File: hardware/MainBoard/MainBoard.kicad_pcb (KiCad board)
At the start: 2 copper layers, 50 x 80 mm, 29 parts, among them J101 Servo, J102 Relay, J103 MotorDriver, J104 MPU9250, J105 PicoBATT+, J106 Tachometer, J201 Micro_SD_Card, SW101 Reset, SW102 SW_Pico, SW103 SW_BATT

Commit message: ちょっと位置修正と，SDの接続ピン変更
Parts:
- moved C201 8.51 mm to (141.8, 97.5), turned to -90 degrees
- moved C202 8.50 mm to (138.7, 97.5), turned to -90 degrees
- moved R201 1.44 mm to (129.2, 106.2)
- moved R202 1.44 mm to (129.2, 103.7)
- moved R203 1.44 mm to (129.2, 101.2)
- moved R204 1.44 mm to (129.2, 98.7)
- moved R102 0.70 mm to (139.0, 111.7)
- moved SW103 0.63 mm to (162.6, 51.7)
- moved SW102 0.60 mm to (162.6, 63.5)
- moved D101 0.50 mm to (120.1, 86.8)
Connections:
- A101 pad 22: /CS -> /CLK
- A101 pad 24: /CLK -> /MOSI
- A101 pad 25: /MOSI -> /CS
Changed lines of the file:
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@@
 	(footprint "Resistor_THT:R_Axial_DIN0204_L3.6mm_D1.6mm_P5.08mm_Horizontal"
 		(layer "F.Cu")
-		(at 130.42 107)
+		(at 129.22 106.2)
 		(descr "Resistor, Axial_DIN0204 series, Axial, Horizontal, pin pitch=5.08mm, 0.167W, length*diameter=3.6*1.6mm^2, http://cdn-reichelt.de/documents/datenblatt/B400/1_4W%23YAG.pdf")
 		(tags "Resistor Axial_DIN0204 series Axial Horizontal pin pitch 5.08mm 0.167W length 3.6mm diameter 1.6mm")
@@
 	(footprint "Resistor_THT:R_Axial_DIN0204_L3.6mm_D1.6mm_P5.08mm_Horizontal"
 		(layer "F.Cu")
-		(at 130.42 99.5)
+		(at 129.22 98.7)
 		(descr "Resistor, Axial_DIN0204 series, Axial, Horizontal, pin pitch=5.08mm, 0.167W, length*diameter=3.6*1.6mm^2, http://cdn-reichelt.de/documents/datenblatt/B400/1_4W%23YAG.pdf")
 		(tags "Resistor Axial_DIN0204 series Axial Horizontal pin pitch 5.08mm 0.167W length 3.6mm diameter 1.6mm")
@@
 	(footprint "Resistor_THT:R_Axial_DIN0204_L3.6mm_D1.6mm_P5.08mm_Horizontal"
 		(layer "F.Cu")
-		(at 138.96 111)
+		(at 138.96 111.7)
 		(descr "Resistor, Axial_DIN0204 series, Axial, Horizontal, pin pitch=5.08mm, 0.167W, length*diameter=3.6*1.6mm^2, http://cdn-reichelt.de/documents/datenblatt/B400/1_4W%23YAG.pdf")
 		(tags "Resistor Axial_DIN0204 series Axial Horizontal pin pitch 5.08mm 0.167W length 3.6mm diameter 1.6mm")
@@
 	(footprint "Capacitor_THT:C_Disc_D4.7mm_W2.5mm_P5.00mm"
 		(layer "F.Cu")
-		(at 138.5 106 90)
+		(at 138.7 97.5 -90)
 		(descr "C, Disc series, Radial, pin pitch=5.00mm, diameter*width=4.7*2.5mm^2, Capacitor, http://www.vishay.com/docs/45233/krseries.pdf")
 		(tags "C Disc series Radial pin pitch 5.00mm diameter 4.7mm width 2.5mm Capacitor")
@@
 		(attr through_hole)
 		(fp_line
-			(start 4.97 -1.37)
-			(end 4.97 -1.04)
+			(start 0.03 1.37)
+			(end 0.03 1.04)
 			(stroke
 				(width 0.12)
@@
 		)
 		(fp_line
-			(start 0.03 -1.37)
-			(end 4.97 -1.37)
+			(start 4.97 1.37)
+			(end 0.03 1.37)
 			(stroke
 				(width 0.12)
@@
 		)
 		(fp_line
-			(start 0.03 -1.04)
-			(end 0.03 -1.37)
+			(start 4.97 1.04)
+			(end 4.97 1.37)
 			(stroke
 				(width 0.12)
@@
 		)
 		(fp_line
-			(start 4.97 1.04)
-			(end 4.97 1.37)
+			(start 0.03 -1.04)
+			(end 0.03 -1.37)
 			(stroke
 				(width 0.12)
@@
 		)
 		(fp_line
-			(start 4.97 1.37)
-			(end 0.03 1.37)
+			(start 0.03 -1.37)
+			(end 4.97 -1.37)
 			(stroke
 				(width 0.12)
@@
 		)
 		(fp_line
-			(start 0.03 1.37)
-			(end 0.03 1.04)
+			(start 4.97 -1.37)
+			(end 4.97 -1.04)
 			(stroke
 				(width 0.12)
@@
 		)
 		(pad "1" thru_hole circle
-			(at 0 0 90)
+			(at 0 0 270)
 			(size 1.6 1.6)
 			(drill 0.8)
@@
 		)
 		(pad "2" thru_hole circle
-			(at 5 0 90)
+			(at 5 0 270)
 			(size 1.6 1.6)
 			(drill 0.8)
@@
 	(footprint "Resistor_THT:R_Axial_DIN0204_L3.6mm_D1.6mm_P5.08mm_Horizontal"
 		(layer "F.Cu")
-		(at 130.42 104.5)
+		(at 129.22 103.7)
 		(descr "Resistor, Axial_DIN0204 series, Axial, Horizontal, pin pitch=5.08mm, 0.167W, length*diameter=3.6*1.6mm^2, http://cdn-reichelt.de/documents/datenblatt/B400/1_4W%23YAG.pdf")
 		(tags "Resistor Axial_DIN0204 series Axial Horizontal pin pitch 5.08mm 0.167W length 3.6mm diameter 1.6mm")
@@
 	(footprint "LED_THT:LED_D3.0mm"
 		(layer "F.Cu")
-		(at 120.46 86.5)
+		(at 120.06 86.8)
 		(descr "LED, diameter 3.0mm, 2 pins, generated by kicad-footprint-generator")
 		(tags "LED")
 		(property "Reference" "D101"
-			(at 1.27 -2.96 0)
+			(at -34.66 -1.2 0)
 			(layer "F.SilkS")
 			(effects
@@
 		(tags "tact sw push 6mm")
 		(property "Reference" "SW101"
-			(at 3.25 -2 0)
+			(at -22.85 6.65 0)
 			(layer "F.SilkS")
 			(effects
@@
 	(footprint "Resistor_THT:R_Axial_DIN0204_L3.6mm_D1.6mm_P5.08mm_Horizontal"
 		(layer "F.Cu")
-		(at 130.42 102)
+		(at 129.22 101.2)
 		(descr "Resistor, Axial_DIN0204 series, Axial, Horizontal, pin pitch=5.08mm, 0.167W, length*diameter=3.6*1.6mm^2, http://cdn-reichelt.de/documents/datenblatt/B400/1_4W%23YAG.pdf")
 		(tags "Resistor Axial_DIN0204 series Axial Horizontal pin pitch 5.08mm 0.167W length 3.6mm diameter 1.6mm")
@@
 	(footprint "Capacitor_THT:C_Disc_D4.7mm_W2.5mm_P5.00mm"
 		(layer "F.Cu")
-		(at 141.5 106 90)
+		(at 141.8 97.5 -90)
 		(descr "C, Disc series, Radial, pin pitch=5.00mm, diameter*width=4.7*2.5mm^2, Capacitor, http://www.vishay.com/docs/45233/krseries.pdf")
 		(tags "C Disc series Radial pin pitch 5.00mm diameter 4.7mm width 2.5mm Capacitor")
@@
 		(attr through_hole)
 		(fp_line
-			(start 4.97 -1.37)
-			(end 4.97 -1.04)
+			(start 0.03 1.37)
+			(end 0.03 1.04)
 			(stroke
 				(width 0.12)
@@
 		)
 		(fp_line
-			(start 0.03 -1.37)
-			(end 4.97 -1.37)
+			(start 4.97 1.37)
+			(end 0.03 1.37)
 			(stroke
 				(width 0.12)
@@
 		)
 		(fp_line
-			(start 0.03 -1.04)
-			(end 0.03 -1.37)
+			(start 4.97 1.04)
+			(end 4.97 1.37)
 			(stroke
 				(width 0.12)
@@
 		)
 		(fp_line
-			(start 4.97 1.04)
-			(end 4.97 1.37)
+			(start 0.03 -1.04)
+			(end 0.03 -1.37)
 			(stroke
 				(width 0.12)
@@
 		)
 		(fp_line
-			(start 4.97 1.37)
-			(end 0.03 1.37)
+			(start 0.03 -1.37)
+			(end 4.97 -1.37)
 			(stroke
 				(width 0.12)
@@
 		)
 		(fp_line
-			(start 0.03 1.37)
-			(end 0.03 1.04)
+			(start 4.97 -1.37)
+			(end 4.97 -1.04)
 			(stroke
 				(width 0.12)
@@
 		)
 		(pad "1" thru_hole circle
-			(at 0 0 90)
+			(at 0 0 270)
 			(size 1.6 1.6)
 			(drill 0.8)
@@
 		)
 		(pad "2" thru_hole circle
-			(at 5 0 90)
+			(at 5 0 270)
 			(size 1.6 1.6)
 			(drill 0.8)
@@
 	(footprint "Button_Switch_THT:SW_Slide_SPDT_Angled_CK_OS102011MA1Q"
 		(layer "F.Cu")
-		(at 162 51.5 90)
+		(at 162.6 51.7 90)
 		(descr "CuK miniature slide switch, OS series, SPDT, right angle, http://www.ckswitches.com/media/1428/os.pdf")
 		(tags "switch SPDT")
@@
 		(tags "connector JST XH vertical")
 		(property "Reference" "J101"
-			(at 2.5 -3.55 90)
+			(at 2.2 -42.4 90)
 			(layer "F.SilkS")
 			(effects
@@
 	(footprint "Button_Switch_THT:SW_Slide_SPDT_Angled_CK_OS102011MA1Q"
 		(layer "F.Cu")
-		(at 162 63.5 90)
+		(at 162.6 63.5 90)
 		(descr "CuK miniature slide switch, OS series, SPDT, right angle, http://www.ckswitches.com/media/1428/os.pdf")
 		(tags "switch SPDT")
@@
 		(tags "module usb pcb antenna")
 		(property "Reference" "A101"
-			(at 11.7475 24.765 0)
+			(at 53.5 8 0)
 			(unlocked yes)
 			(layer "F.SilkS")
@@
 			(layers "*.Cu" "*.Mask")
 			(remove_unused_layers no)
-			(net 35 "/CS")
+			(net 3 "/CLK")
 			(pinfunction "GPIO17")
 			(pintype "bidirectional")
@@
 			(layers "F.Cu" "F.Mask")
 			(roundrect_rratio 0.5)
-			(net 35 "/CS")
+			(net 3 "/CLK")
 			(pinfunction "GPIO17")
 			(pintype "bidirectional")
@@
 			(layers "*.Cu" "*.Mask")
 			(remove_unused_layers no)
-			(net 3 "/CLK")
+			(net 2 "/MOSI")
 			(pinfunction "GPIO18")
 			(pintype "bidirectional")
@@
 			(layers "F.Cu" "F.Mask")
 			(roundrect_rratio 0.5)
-			(net 3 "/CLK")
+			(net 2 "/MOSI")
 			(pinfunction "GPIO18")
 			(pintype "bidirectional")
@@
 			(layers "*.Cu" "*.Mask")
 			(remove_unused_layers no)
-			(net 2 "/MOSI")
+			(net 35 "/CS")
 			(pinfunction "GPIO19")
 			(pintype "bidirectional")
@@
 			(layers "F.Cu" "F.Mask")
 			(roundrect_rratio 0.5)
-			(net 2 "/MOSI")
+			(net 35 "/CS")
 			(pinfunction "GPIO19")
 			(pintype "bidirectional")

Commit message: コネクタ類をまとめた
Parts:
- added REF**: MountingHole_3.2mm_M3, MountingHole:MountingHole_3.2mm_M3, F.Cu at (143.5, 108.3)
- added REF**: MountingHole_3.2mm_M3, MountingHole:MountingHole_3.2mm_M3, F.Cu at (123.2, 108.3)
- moved D101 40.2 mm to (160.2, 86.2)
- moved R103 38.5 mm to (158.0, 78.1)
- moved R102 38.3 mm to (153.0, 76.0)
- moved J106 37.1 mm to (121.1, 92.1)
- moved D102 36.7 mm to (160.2, 77.1)
- moved D103 30.8 mm to (160.2, 81.6)
- moved R101 30.7 mm to (153.0, 80.2), turned to 0 degrees
- moved C202 6.09 mm to (137.2, 103.4), turned to 0 degrees
- moved C201 5.44 mm to (137.2, 100.4), turned to 0 degrees
- moved J104 3.51 mm to (121.9, 96.9)
- moved C203 2.90 mm to (144.4, 100.8), turned to -90 degrees
- moved J201 2.38 mm to (156.1, 98.2)
- moved R201 2.20 mm to (129.2, 108.4)
- moved R202 2.20 mm to (129.2, 105.9)
- moved R203 2.20 mm to (129.2, 103.4)
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
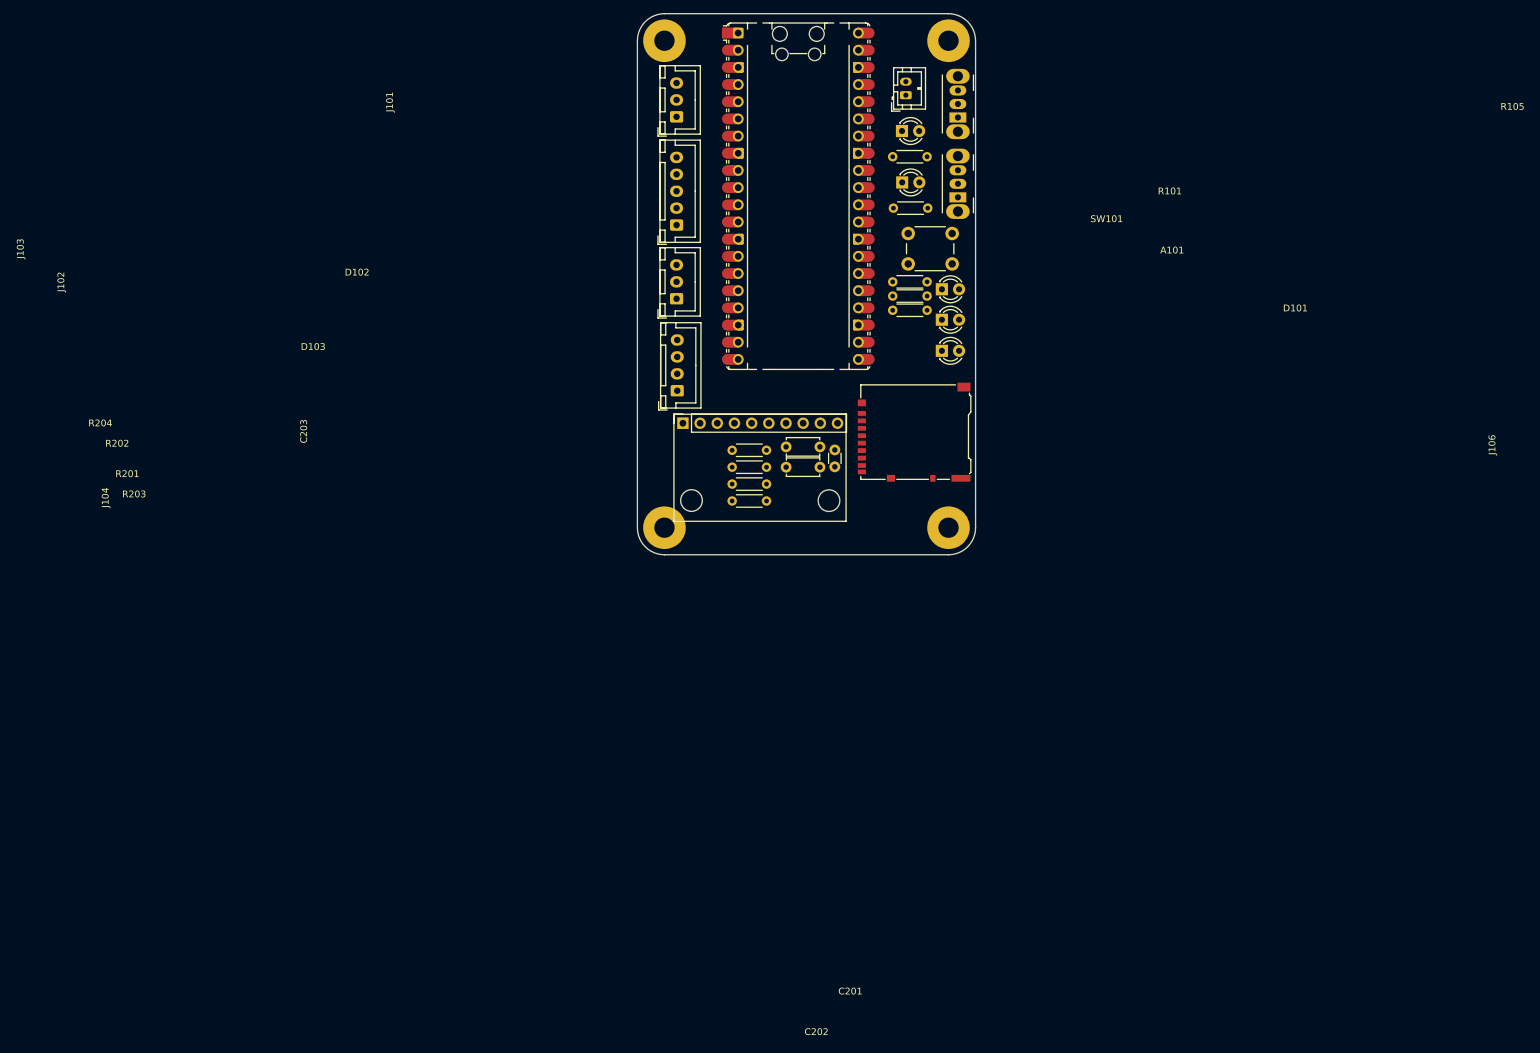
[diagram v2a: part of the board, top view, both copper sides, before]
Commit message: PCBで配線少し
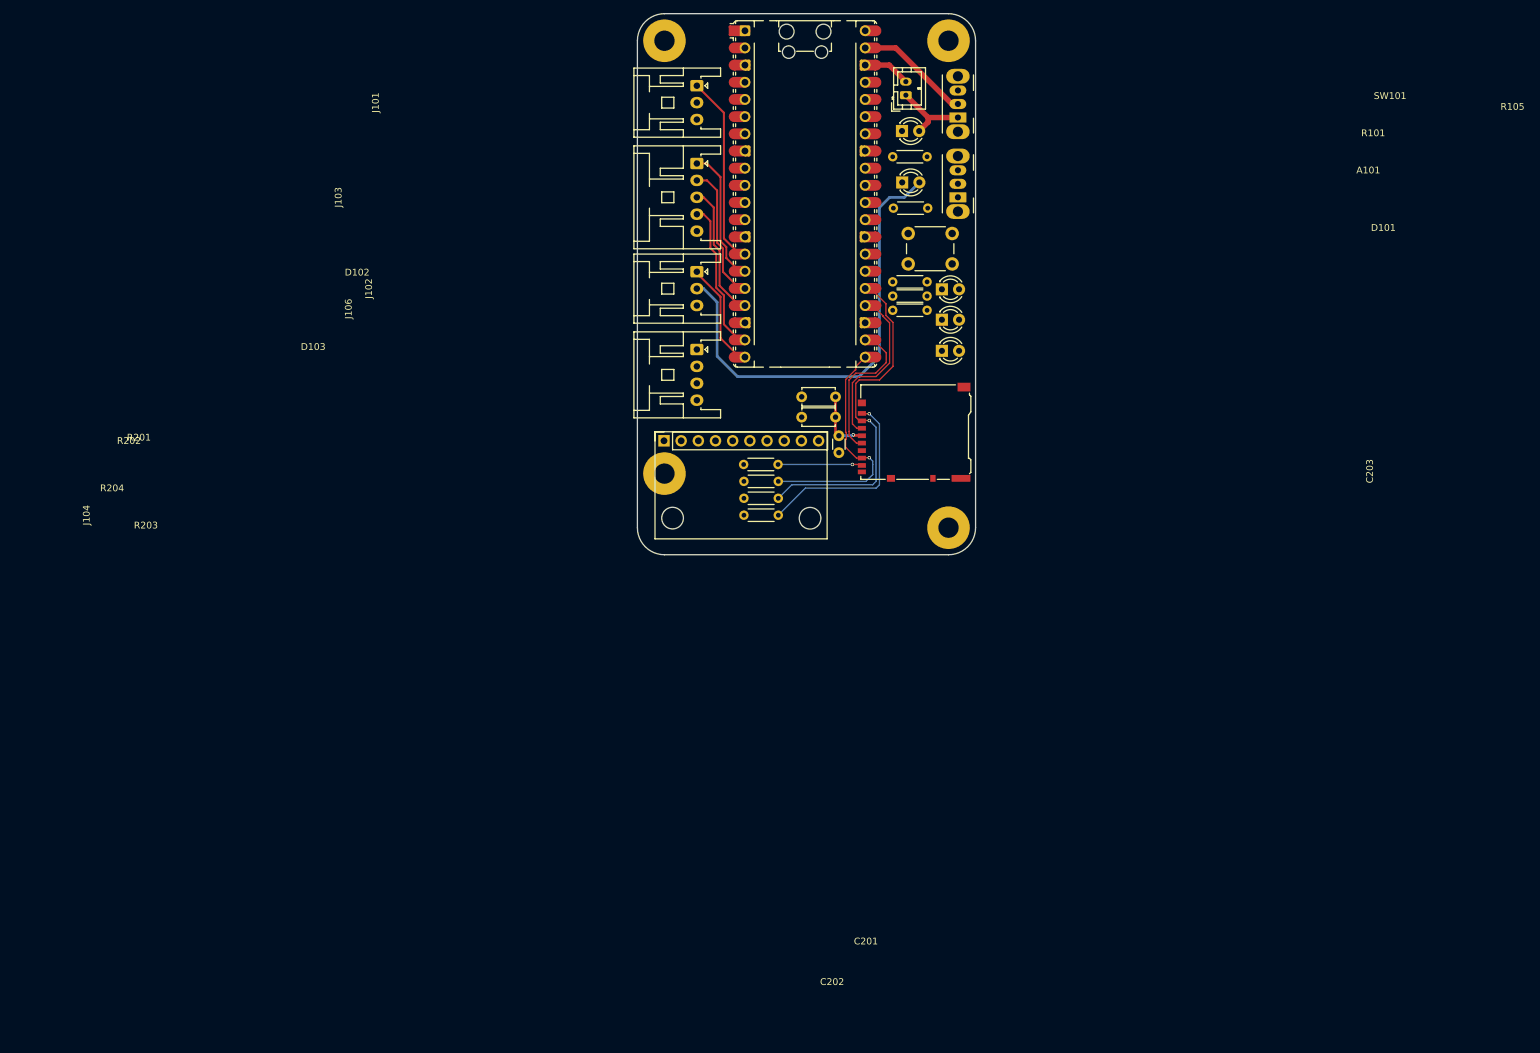
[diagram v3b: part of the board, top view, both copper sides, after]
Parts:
- J101, J102: footprint Connector_JST:JST_XH_B3B-XH-A_1x03_P2.50mm_Vertical -> Connector_JST:JST_XA_S03B-XASK-1_1x03_P2.50mm_Horizontal
- J103: footprint Connector_JST:JST_XH_B5B-XH-A_1x05_P2.50mm_Vertical -> Connector_JST:JST_XA_S05B-XASK-1_1x05_P2.50mm_Horizontal
- J106: footprint Connector_JST:JST_XH_B4B-XH-A_1x04_P2.50mm_Vertical -> Connector_JST:JST_XA_S04B-XASK-1_1x04_P2.50mm_Horizontal
- moved R204 9.76 mm to (131.0, 110.5)
- moved J103 9.58 mm to (124.0, 58.5), turned to -90 degrees
- moved C201 7.75 mm to (139.5, 93.0)
- moved C202 7.75 mm to (139.5, 96.0)
- moved J106 6.75 mm to (124.0, 86.0), turned to -90 degrees
- moved R201 5.66 mm to (130.9, 103.0)
- moved J101 5.49 mm to (124.0, 47.0), turned to -90 degrees
- moved J102 5.00 mm to (124.0, 74.5), turned to -90 degrees
- moved R203 4.92 mm to (131.0, 108.0)
- moved REF** 3.82 mm to (120.4, 110.9)
- moved J104 3.82 mm to (119.1, 99.5)
- moved REF** 3.82 mm to (140.7, 111.0)
- moved R202 1.79 mm to (131.0, 105.5)
- moved A101 1.06 mm to (140.0, 63.0)
- moved C203 0.72 mm to (145.0, 101.2), turned to 90 degrees
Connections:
- J101 pad 1: GND -> /Servo_S
- J101 pad 3: /Servo_S -> GND
- J102 pad 1: GND -> /Relay_S
- J102 pad 3: /Relay_S -> GND
- J103 pad 1: GND -> /IN1
- J103 pad 2: /IN4 -> /IN2
- J103 pad 4: /IN2 -> /IN4
- J103 pad 5: /IN1 -> GND
- J106 pad 1: VDD -> /OUT2
- J106 pad 2: GND -> /OUT1
- J106 pad 3: /OUT1 -> GND
- J106 pad 4: /OUT2 -> VDD
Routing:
- net VDD: track 0.00 -> 77.2 mm, vias 0 -> 1
- net /CS: track 0.00 -> 51.6 mm, vias 0 -> 1
- net /MISO: track 0.00 -> 35.9 mm, vias 0 -> 1
- net Net-(J201-DAT2): track 0.00 -> 29.1 mm, vias 0 -> 1
- net /Servo_S: track 0.00 -> 27.5 mm
- net /MOSI: track 0.00 -> 25.1 mm
- net /CLK: track 0.00 -> 22.5 mm
- net /IN4: track 0.00 -> 21.8 mm
- net /IN2: track 0.00 -> 19.5 mm
- net /IN1: track 0.00 -> 19.4 mm
- net /IN3: track 0.00 -> 19.2 mm
- net Net-(A101-VSYS): track 0.00 -> 16.3 mm
- net /Relay_S: track 0.00 -> 15.2 mm
- net Net-(J201-DAT1): track 0.00 -> 12.5 mm, vias 0 -> 1
- net Net-(D104-A): track 0.00 -> 11.6 mm
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
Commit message: 配置をちょっとだけ変更
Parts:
- moved R101 6.70 mm to (155.0, 86.6), turned to 90 degrees
- moved R103 3.60 mm to (157.2, 81.6), turned to -90 degrees
- moved R102 3.45 mm to (152.7, 72.6), turned to -90 degrees
- moved SW101 0.20 mm to (161.9, 73.3)

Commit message: 線のでこぼこを修正。いくつか0.2mmで接続。
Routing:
- net /OUT2: track 0.00 -> 62.9 mm, vias 0 -> 1
- net /SDA: track 0.00 -> 58.6 mm, vias 0 -> 1
- net /OUT1: track 0.00 -> 46.9 mm, vias 0 -> 1
- net Net-(A101-3V3_EN): track 0.00 -> 24.7 mm
- net Net-(D104-K): track 0.00 -> 4.37 mm
- net Net-(D105-K): track 0.00 -> 4.34 mm
- net Net-(D102-K): track 0.00 -> 0.76 mm

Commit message: 一応、未配線0になった
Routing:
- net /SCL: track 0.00 -> 62.6 mm, vias 0 -> 1
- net /Relay_S: track 15.2 -> 58.8 mm, vias 0 -> 1
- net /ERROR: track 0.00 -> 42.6 mm
- net /STAT: track 0.00 -> 41.1 mm
- net Net-(A101-RUN): track 0.00 -> 14.2 mm
- net Net-(D101-K): track 0.00 -> 7.18 mm
- net Net-(D102-K): track 0.76 -> 7.75 mm
- net /OUT2: track 62.9 -> 59.7 mm
- net Net-(D103-K): track 0.00 -> 3.03 mm
- net Net-(J201-DAT2): track 29.1 -> 28.3 mm
- net /CS: track 51.6 -> 51.0 mm
